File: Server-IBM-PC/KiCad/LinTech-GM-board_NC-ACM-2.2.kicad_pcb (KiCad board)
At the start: 2 copper layers, 168.9 x 106.7 mm, 78 parts, among them Q1 12000 KHz, X7 Conn_02x03_Counter_Clockwise

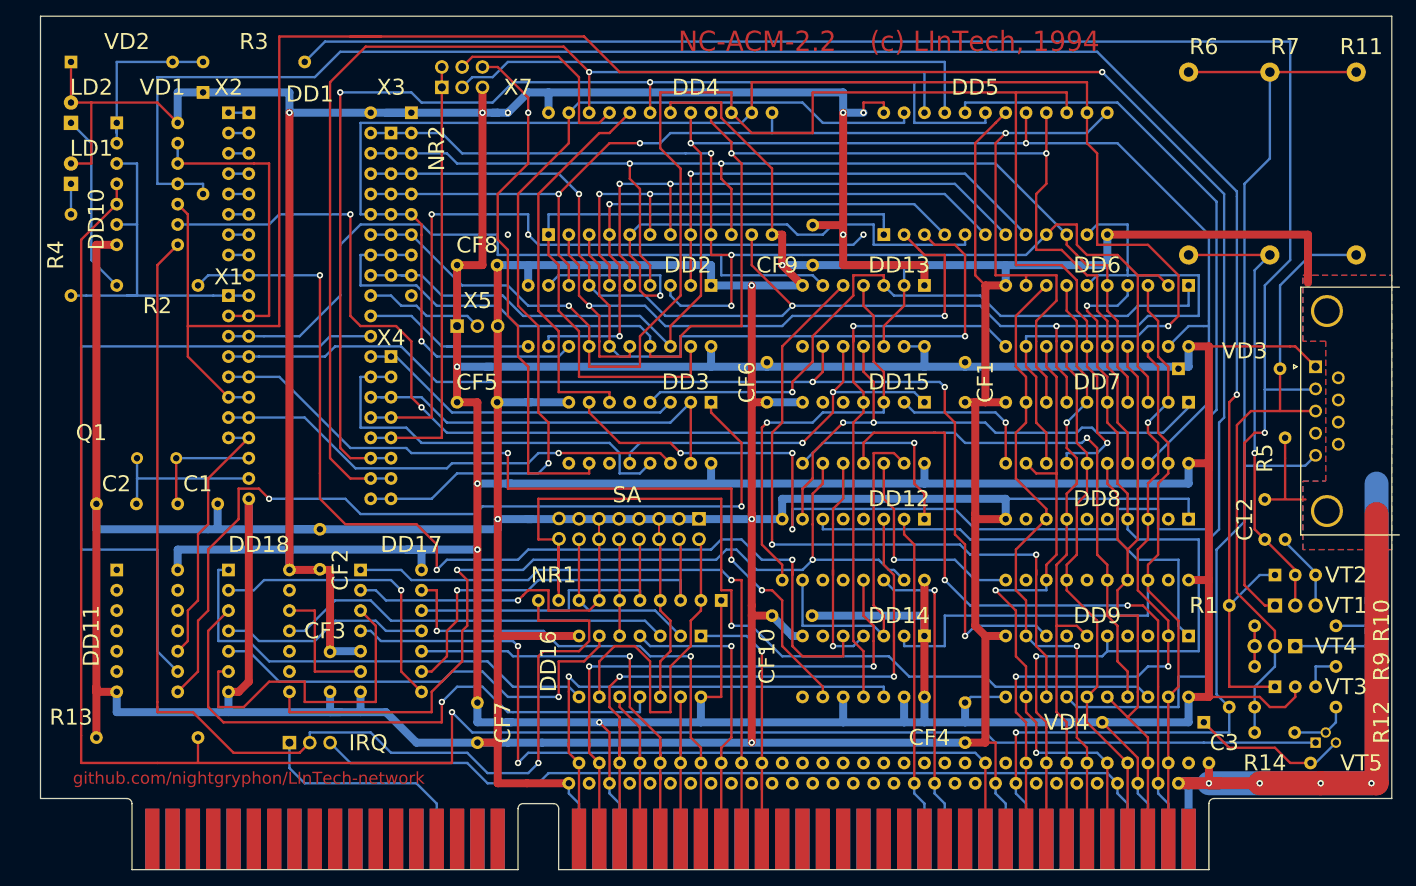
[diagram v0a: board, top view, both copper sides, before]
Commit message: FIX DD9 pin 13 wire, add R15 placeholder
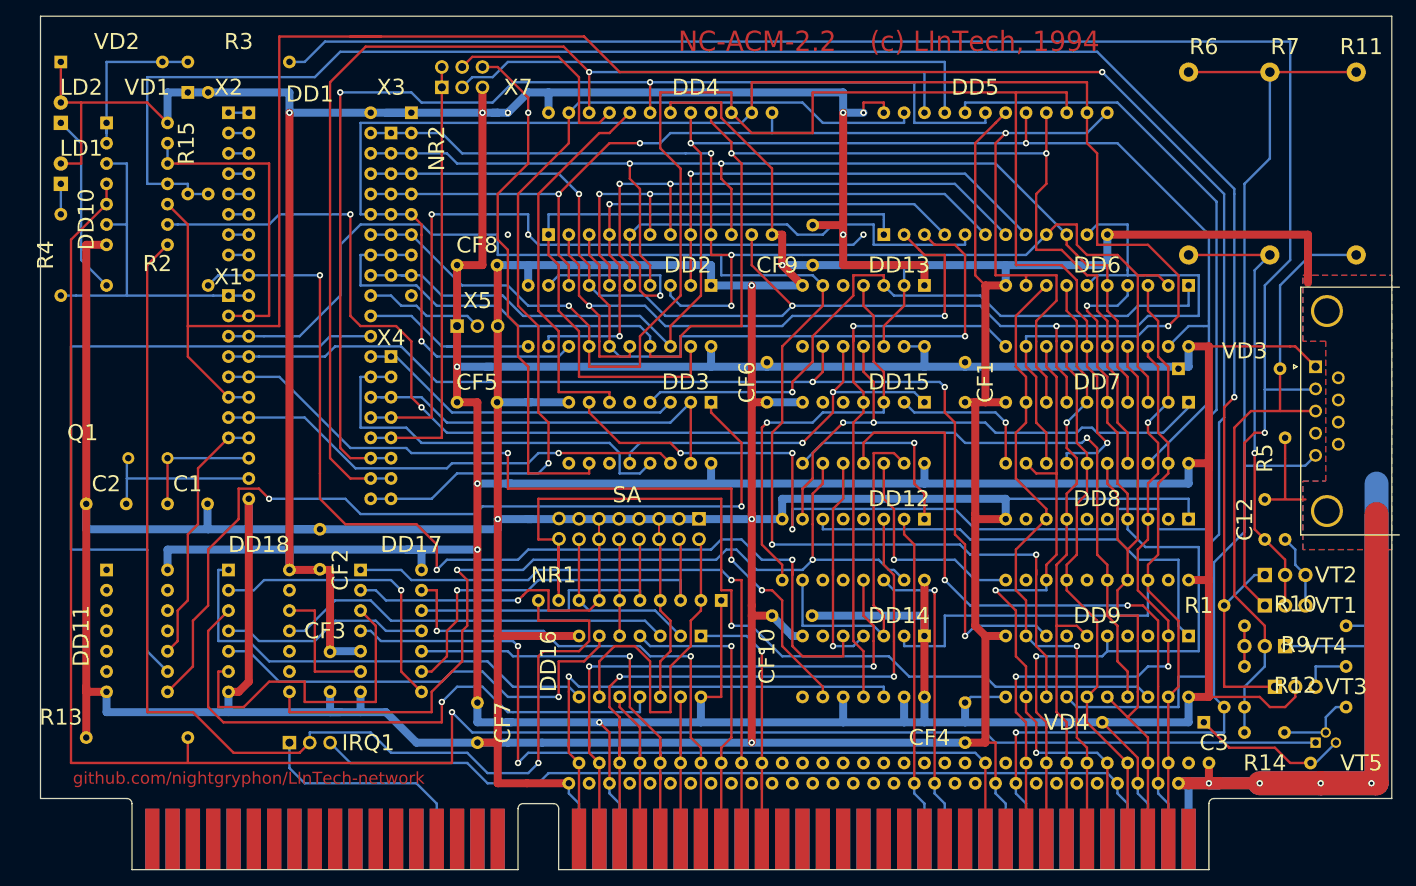
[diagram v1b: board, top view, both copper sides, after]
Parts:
- added R15: 4.9K, lib:R_Axial_DIN0309_L9.0mm_D3.2mm_P12.70mm_Horizontal, F.Cu at (80.6, 48.9)
- R10, R12, R2, R9: footprint lib:R_Axial_DIN0207_L6.3mm_D2.5mm_P10.16mm_Horizontal -> lib:R_Axial_DIN0309_L9.0mm_D3.2mm_P12.70mm_Horizontal
- moved VD1 1.91 mm to (78.1, 36.2)
- moved R3 1.90 mm to (90.8, 32.4)
- moved C3 1.27 mm to (210.2, 116.2)
- moved DD10 1.27 mm to (67.9, 40.0)
- moved DD11 1.27 mm to (67.9, 95.9)
- moved R10 1.27 mm to (210.2, 102.9)
- moved R12 1.27 mm to (210.2, 113.0)
- moved R2 1.27 mm to (67.9, 60.3)
- moved R9 1.27 mm to (210.2, 108.0)
- moved VT1 1.27 mm to (212.7, 100.3)
- moved VT2 1.27 mm to (212.7, 96.5)
- moved VT4 1.27 mm to (215.3, 105.4)
- moved LD1 1.27 mm to (62.2, 47.6)
- moved LD2 1.27 mm to (62.2, 40.0)
- moved R4 1.27 mm to (62.2, 51.4)
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- renumbered IRQ to IRQ1
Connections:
- DD13 pad 5: Port67_ISA_Data -> Net-(DD13-Pad5)
- DD9 pad 13: Port67_ISA_Data -> MCU_Int0
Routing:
- net Port67_ISA_Data: track 88.6 -> 0.00 mm, vias 2 -> 0
- net MCU_Int0: track 89.9 -> 177.4 mm, vias 0 -> 2
- net GND: track 985.7 -> 989.6 mm
- net /DD10_Out11: track 239.1 -> 242.3 mm
- net +5V: track 858.6 -> 861.1 mm
- net Net-(C3-Pad2): track 7.59 -> 10.1 mm
- net MCU_PSEN: track 87.9 -> 89.2 mm
- net IRQ: track 145.5 -> 146.8 mm
- net /MCU_RST: track 131.8 -> 130.5 mm
- net Net-(C2-Pad2): track 19.0 -> 20.2 mm
- net MCU_TXD: track 38.1 -> 39.4 mm
- net Net-(R9-Pad2): track 5.08 -> 6.35 mm
- net Net-(DD10-Pad4): track 239.6 -> 240.9 mm
- net ISA_IRQ_EN_BIT: track 172.9 -> 174.2 mm
- net Net-(C1-Pad1): track 14.9 -> 15.9 mm
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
